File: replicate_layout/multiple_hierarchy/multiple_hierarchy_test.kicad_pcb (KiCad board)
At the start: 2 copper layers, 72 parts, among them J1001 Pusa_4mm, J1002 Pusa_4mm, J201 Pusa_4mm, J202 Pusa_4mm, J601 Pusa_4mm, J602 Pusa_4mm, Q1101 CSD19531KCS, Q1102 CSD19531KCS, Q1301 CSD19531KCS, Q1302 CSD19531KCS, Q1401 CSD19531KCS, Q1402 CSD19531KCS, Q301 CSD19531KCS, Q302 CSD19531KCS, Q501 CSD19531KCS, Q502 CSD19531KCS, Q701 CSD19531KCS, Q702 CSD19531KCS, Q901 CSD19531KCS, Q902 CSD19531KCS, U101 TMS320F28027DA, U1101 IR2181, U1201 INA240, U1301 IR2181, U1401 IR2181, U301 IR2181, U401 INA240, U501 IR2181, U701 IR2181, U801 INA240, U901 IR2181

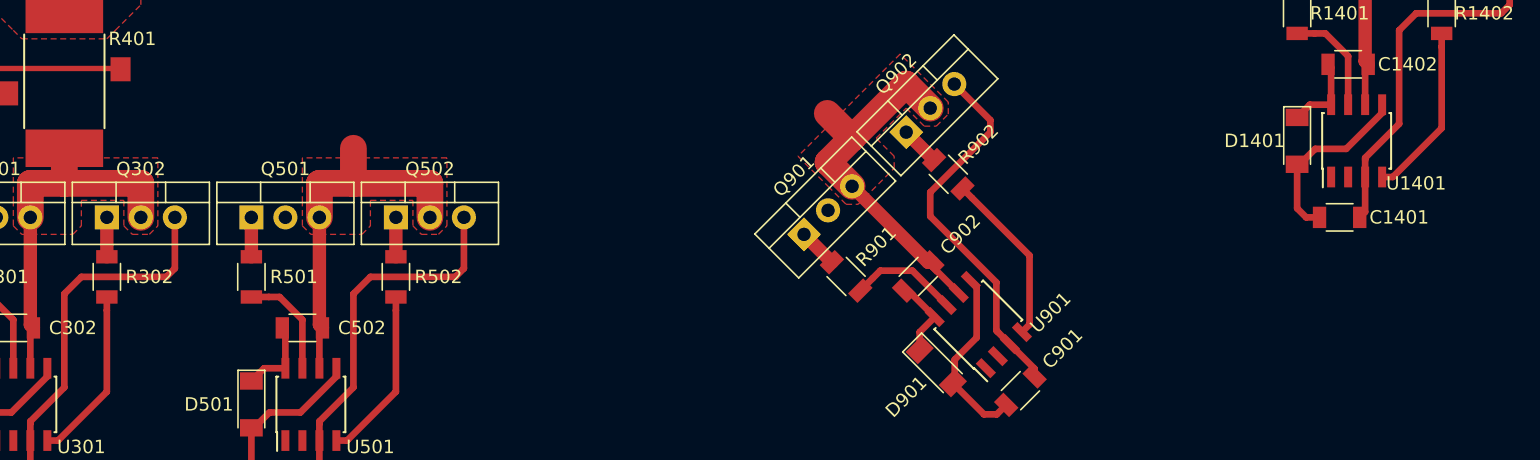
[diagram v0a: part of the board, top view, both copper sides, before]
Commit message: replicate all drawings
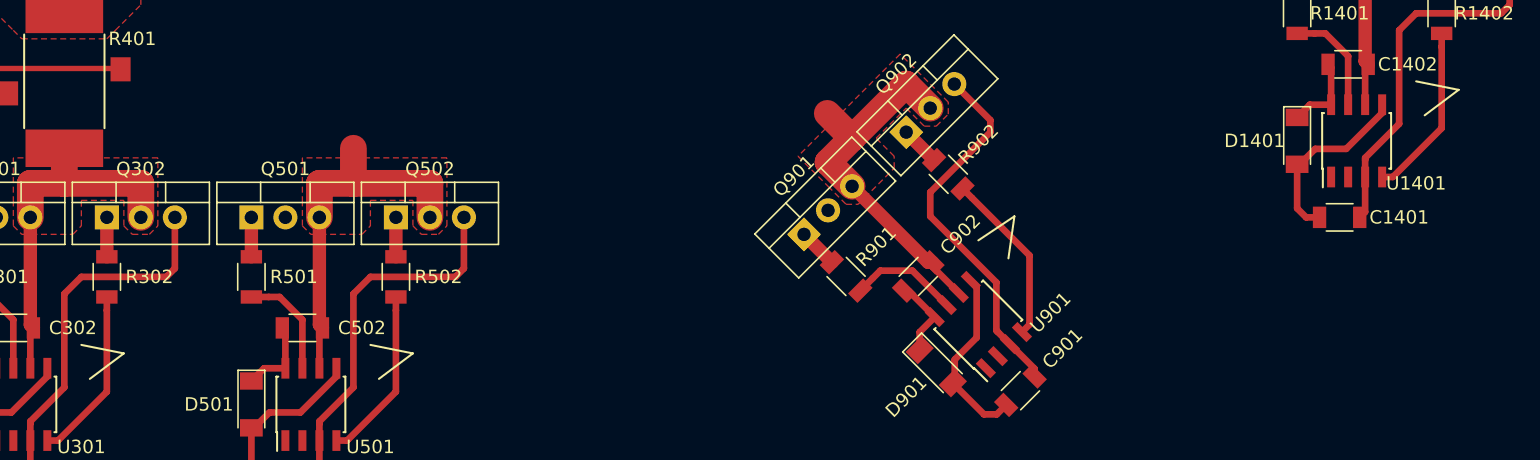
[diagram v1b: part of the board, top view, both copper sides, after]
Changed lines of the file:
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@@
-(kicad_pcb (version 20171130) (host pcbnew "(5.1.0)-1")
+(kicad_pcb (version 20171130) (host pcbnew "(5.1.0-rc2-4-g73f0b3087)")
   (general
     (thickness 1.6)
-    (drawings 4)
+    (drawings 20)
     (tracks 177)
     (zones 0)
@@
     )
   )
+  (gr_line (start 194.31 43.815) (end 198.12 41.91) (layer F.Fab) (width 0.15))
+  (gr_line (start 198.12 41.91) (end 198.755 43.815) (layer F.Fab) (width 0.15))
+  (gr_line (start 197.485 43.815) (end 194.31 43.18) (layer F.SilkS) (width 0.15))
+  (gr_line (start 197.485 43.815) (end 194.945 45.72) (layer F.SilkS) (width 0.15))
+  (gr_line (start 162.060384 55.508025) (end 163.407422 51.46691) (layer F.Fab) (width 0.15))
+  (gr_line (start 163.407422 51.46691) (end 165.203473 52.364935) (layer F.Fab) (width 0.15))
+  (gr_line (start 164.305448 53.262961) (end 161.611371 55.059012) (layer F.SilkS) (width 0.15))
+  (gr_line (start 164.305448 53.262961) (end 163.856435 56.406051) (layer F.SilkS) (width 0.15))
+  (gr_line (start 116.205 63.5) (end 120.015 61.595) (layer F.Fab) (width 0.15))
+  (gr_line (start 120.015 61.595) (end 120.65 63.5) (layer F.Fab) (width 0.15))
+  (gr_line (start 119.38 63.5) (end 116.205 62.865) (layer F.SilkS) (width 0.15))
+  (gr_line (start 119.38 63.5) (end 116.84 65.405) (layer F.SilkS) (width 0.15))
   (gr_text A (at 198.12 46.99 90) (layer F.Fab)
     (effects (font (size 3 3) (thickness 0.5)))
@@
     (effects (font (size 3 3) (thickness 0.5)))
   )
+  (gr_line (start 97.79 63.5) (end 95.25 65.405) (layer F.SilkS) (width 0.15))
+  (gr_line (start 97.79 63.5) (end 94.615 62.865) (layer F.SilkS) (width 0.15))
+  (gr_line (start 98.425 61.595) (end 99.06 63.5) (layer F.Fab) (width 0.15))
+  (gr_line (start 94.615 63.5) (end 98.425 61.595) (layer F.Fab) (width 0.15))
   (gr_text A (at 98.425 66.675 90) (layer F.Fab)
     (effects (font (size 3 3) (thickness 0.5)))

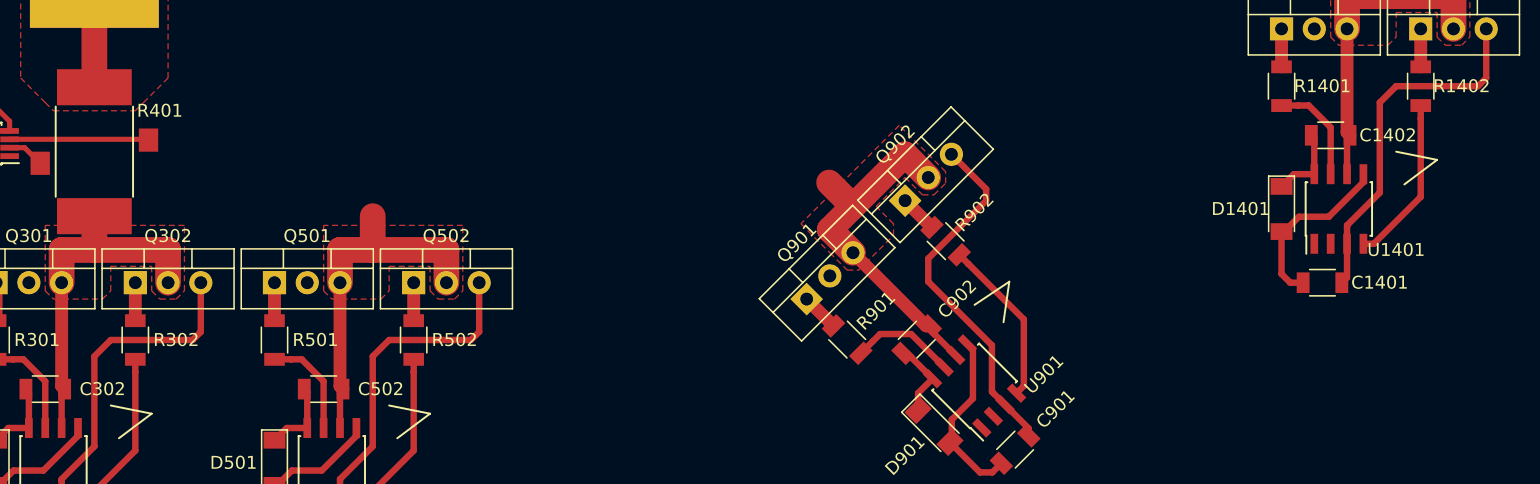
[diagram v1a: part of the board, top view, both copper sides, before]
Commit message: SImplified text replication
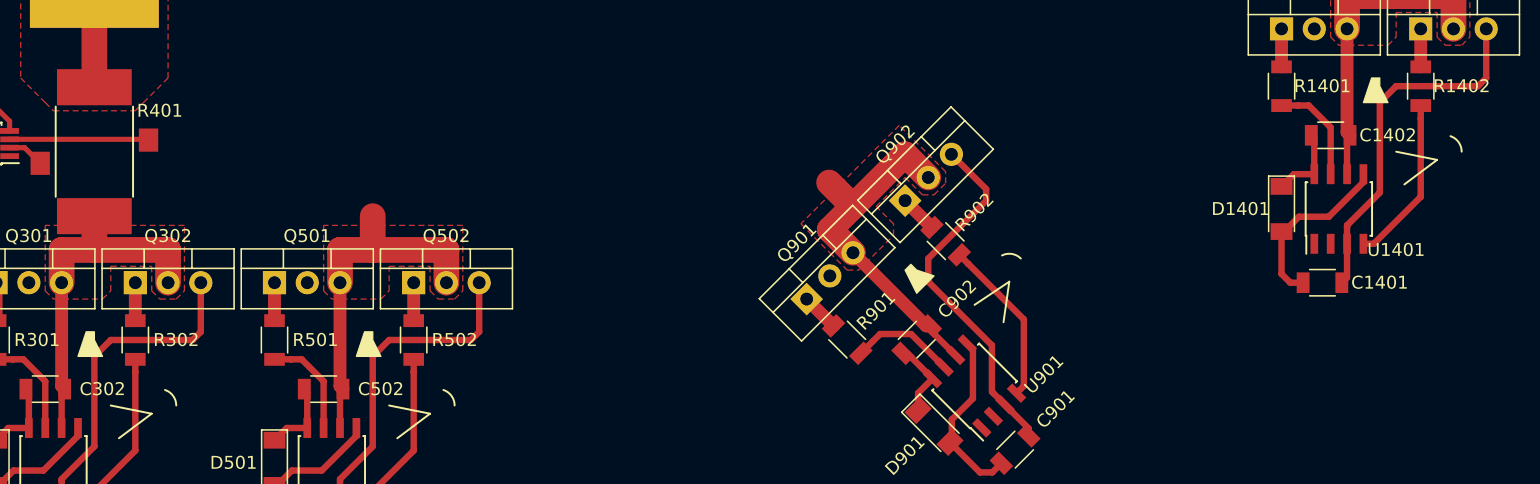
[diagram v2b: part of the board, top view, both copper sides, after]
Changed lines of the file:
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@@
   (general
     (thickness 1.6)
-    (drawings 20)
+    (drawings 32)
     (tracks 177)
     (zones 0)
@@
   (gr_line (start 197.485 43.815) (end 194.31 43.18) (layer F.SilkS) (width 0.15))
   (gr_line (start 197.485 43.815) (end 194.945 45.72) (layer F.SilkS) (width 0.15))
-  (gr_line (start 162.060384 55.508025) (end 163.407422 51.46691) (layer F.Fab) (width 0.15))
-  (gr_line (start 163.407422 51.46691) (end 165.203473 52.364935) (layer F.Fab) (width 0.15))
-  (gr_line (start 164.305448 53.262961) (end 161.611371 55.059012) (layer F.SilkS) (width 0.15))
-  (gr_line (start 164.305448 53.262961) (end 163.856435 56.406051) (layer F.SilkS) (width 0.15))
+  (gr_circle (center 199.39 39.37) (end 200.025 40.005) (layer F.Fab) (width 0.15))
+  (gr_arc (start 198.12 43.18) (end 199.39 43.18) (angle -71.56505118) (layer F.SilkS) (width 0.15))
+  (gr_poly (pts (xy 192.405 37.465) (xy 191.77 39.37) (xy 193.675 39.37) (xy 193.04 38.1) (xy 193.04 37.465)) (layer F.SilkS) (width 0.1))
+  (gr_line (start 162.060384 55.508026) (end 163.407423 51.46691) (layer F.Fab) (width 0.15))
+  (gr_line (start 163.407423 51.46691) (end 165.203474 52.364936) (layer F.Fab) (width 0.15))
+  (gr_line (start 164.305448 53.262962) (end 161.611371 55.059013) (layer F.SilkS) (width 0.15))
+  (gr_line (start 164.305448 53.262962) (end 163.856435 56.406051) (layer F.SilkS) (width 0.15))
+  (gr_circle (center 162.509397 48.772834) (end 163.407423 48.772834) (layer F.Fab) (width 0.15))
+  (gr_arc (start 164.305448 52.364936) (end 165.203474 51.46691) (angle -71.56505118) (layer F.SilkS) (width 0.15))
+  (gr_poly (pts (xy 156.223218 52.364936) (xy 157.121243 54.160987) (xy 158.468282 52.813949) (xy 157.121243 52.364936) (xy 156.672231 51.915923)) (layer F.SilkS) (width 0.1))
   (gr_line (start 116.205 63.5) (end 120.015 61.595) (layer F.Fab) (width 0.15))
   (gr_line (start 120.015 61.595) (end 120.65 63.5) (layer F.Fab) (width 0.15))
   (gr_line (start 119.38 63.5) (end 116.205 62.865) (layer F.SilkS) (width 0.15))
   (gr_line (start 119.38 63.5) (end 116.84 65.405) (layer F.SilkS) (width 0.15))
+  (gr_circle (center 121.285 59.055) (end 121.92 59.69) (layer F.Fab) (width 0.15))
+  (gr_arc (start 120.015 62.865) (end 121.285 62.865) (angle -71.56505118) (layer F.SilkS) (width 0.15))
+  (gr_poly (pts (xy 114.3 57.15) (xy 113.665 59.055) (xy 115.57 59.055) (xy 114.935 57.785) (xy 114.935 57.15)) (layer F.SilkS) (width 0.1))
   (gr_text A (at 198.12 46.99 90) (layer F.Fab)
     (effects (font (size 3 3) (thickness 0.5)))
   )
-  (gr_text A (at 166.999525 55.059012 135) (layer F.Fab)
+  (gr_text A (at 166.999525 55.059013 135) (layer F.Fab)
     (effects (font (size 3 3) (thickness 0.5)))
   )
@@
     (effects (font (size 3 3) (thickness 0.5)))
   )
+  (gr_poly (pts (xy 92.71 57.15) (xy 92.075 59.055) (xy 93.98 59.055) (xy 93.345 57.785) (xy 93.345 57.15)) (layer F.SilkS) (width 0.1))
+  (gr_arc (start 98.425 62.865) (end 99.695 62.865) (angle -71.56505118) (layer F.SilkS) (width 0.15))
+  (gr_circle (center 99.695 59.055) (end 100.33 59.69) (layer F.Fab) (width 0.15))
   (gr_line (start 97.79 63.5) (end 95.25 65.405) (layer F.SilkS) (width 0.15))
   (gr_line (start 97.79 63.5) (end 94.615 62.865) (layer F.SilkS) (width 0.15))
@@
     )
   )
+  (zone (net 0) (net_name "") (layer F.Cu) (hatch edge 0.508)
+    (connect_pads (clearance 0.508))
+    (min_thickness 0.254)
+    (keepout (tracks not_allowed) (vias not_allowed) (copperpour not_allowed))
+    (fill (arc_segments 32) (thermal_gap 0.508) (thermal_bridge_width 0.508))
+    (polygon
+      (pts
+        (xy 187.325 36.83) (xy 189.23 36.83) (xy 189.23 38.735) (xy 187.325 38.735)
+      )
+    )
+  )
   (zone (net 0) (net_name "") (layer F.Mask) (hatch edge 0.508)
     (connect_pads (clearance 0.508))
@@
     )
   )
+  (zone (net 0) (net_name "") (layer F.Cu) (hatch edge 0.508)
+    (connect_pads (clearance 0.508))
+    (min_thickness 0.254)
+    (keepout (tracks not_allowed) (vias not_allowed) (copperpour not_allowed))
+    (fill (arc_segments 32) (thermal_gap 0.508) (thermal_bridge_width 0.508))
+    (polygon
+      (pts
+        (xy 152.182102 55.508025) (xy 153.52914 54.160987) (xy 154.876179 55.508025) (xy 153.52914 56.855064)
+      )
+    )
+  )
   (zone (net 0) (net_name "") (layer F.Mask) (hatch edge 0.508)
     (connect_pads (clearance 0.508))
@@
     )
   )
+  (zone (net 0) (net_name "") (layer F.Cu) (hatch edge 0.508)
+    (connect_pads (clearance 0.508))
+    (min_thickness 0.254)
+    (keepout (tracks not_allowed) (vias not_allowed) (copperpour not_allowed))
+    (fill (arc_segments 32) (thermal_gap 0.508) (thermal_bridge_width 0.508))
+    (polygon
+      (pts
+        (xy 109.22 56.515) (xy 111.125 56.515) (xy 111.125 58.42) (xy 109.22 58.42)
+      )
+    )
+  )
   (zone (net 0) (net_name "") (layer F.Mask) (hatch edge 0.508)
     (connect_pads (clearance 0.508))
@@
       )
     )
+  )
+  (zone (net 0) (net_name "") (layer F.Cu) (hatch edge 0.508)
+    (connect_pads (clearance 0.508))
+    (min_thickness 0.254)
+    (keepout (tracks not_allowed) (vias not_allowed) (copperpour not_allowed))
+    (fill (arc_segments 32) (thermal_gap 0.508) (thermal_bridge_width 0.508))
+    (polygon
+      (pts
+        (xy 87.63 56.515) (xy 89.535 56.515) (xy 89.535 58.42) (xy 87.63 58.42)
+      )
+    )
